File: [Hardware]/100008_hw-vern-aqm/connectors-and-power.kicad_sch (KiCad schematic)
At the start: 16 parts

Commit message: end of day work
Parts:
- added J?: Conn_01x03_Pin, symbol Connector:Conn_01x03_Pin
- added J?: Conn_01x14_Socket, symbol Connector:Conn_01x14_Socket
- added R? (x2): 0R0, Resistor_SMD:R_0603_1608Metric, symbol Device:R
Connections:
- net +3V3: now also R?.2
- net GND: now also J?.2 (Pin_2), J?.3 (Pin_3)
- net VBUS: now also R?.2
- net I2C_SDA: now reaches J?.3 (Pin_3)
- net I2C_SCL: now reaches J?.4 (Pin_4)
- new net: J?.1 (Pin_1), R?.1, R?.1
- new net LCD_BACKLIGHT: J?.8 (Pin_8)
- new net LCD_DC/RS: J?.5 (Pin_5)
- new net LCD_RESET: J?.4 (Pin_4)
- new net SPI_MISO: J?.13 (Pin_13)
- new net SPI_MOSI: J?.12 (Pin_12), J?.6 (Pin_6)
- new net SPI_SCK: J?.10 (Pin_10), J?.7 (Pin_7)
- new net SPI_nCS_LCD: J?.3 (Pin_3)
- new net SPI_nCS_TOUCH: J?.11 (Pin_11)
- new net UART0_RX: J?.2 (Pin_2)
- new net UART0_TX: J?.1 (Pin_1)
- no-connect marks 0 -> 4
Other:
- note added: "LCD Display pin header connector - ILI9488 driver"
- note added: "Sensirion SEN54 connector - JST GH 1.25mm"
- note added: "UART Programming header"
- note added: "USB-C Input and data connector"
- moved on the sheet: F?, J?, R?

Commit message: mid day progress
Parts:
- removed J?: USB_C_Receptacle_USB2.0_14P, symbol Connector:USB_C_Receptacle_USB2.0_14P
- added C?: 1u, Capacitor_SMD:C_0805_2012Metric, symbol Device:C
- added D?: ESD5Z3V3, Diode_SMD:D_SOD-523, symbol Diode:ESD5Zxx
- added D?: ESD321, Diode_SMD:D_SOD-523, symbol Diode:ESD5Zxx
- added J?: USB_C_Receptacle_USB2.0_16P, symbol Connector:USB_C_Receptacle_USB2.0_16P
- added R?: 0R0, Resistor_SMD:R_0603_1608Metric, symbol Device:R
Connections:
- net +3V3: now also R?.2; no longer U?.2 (VO)
- net GND: now also J?.A1 (GND), J?.A12 (GND), J?.B1 (GND), J?.B12 (GND), J?.S1 (SHIELD)
- net at R?.1: now also J?.B5 (CC2)
- net at F?.1: now also J?.A4 (VBUS), J?.A9 (VBUS), J?.B4 (VBUS), J?.B9 (VBUS)
- net at R?.1: now also J?.A5 (CC1)
- net at R?.1: now also J?.A6 (D+), J?.B6 (D+)
- net at R?.1: now also J?.A7 (D-), J?.B7 (D-)
- new net: R?.1, U?.2 (VO)
- no-connect marks 4 -> 6
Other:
- moved on the sheet: C?, J?, R?, U?

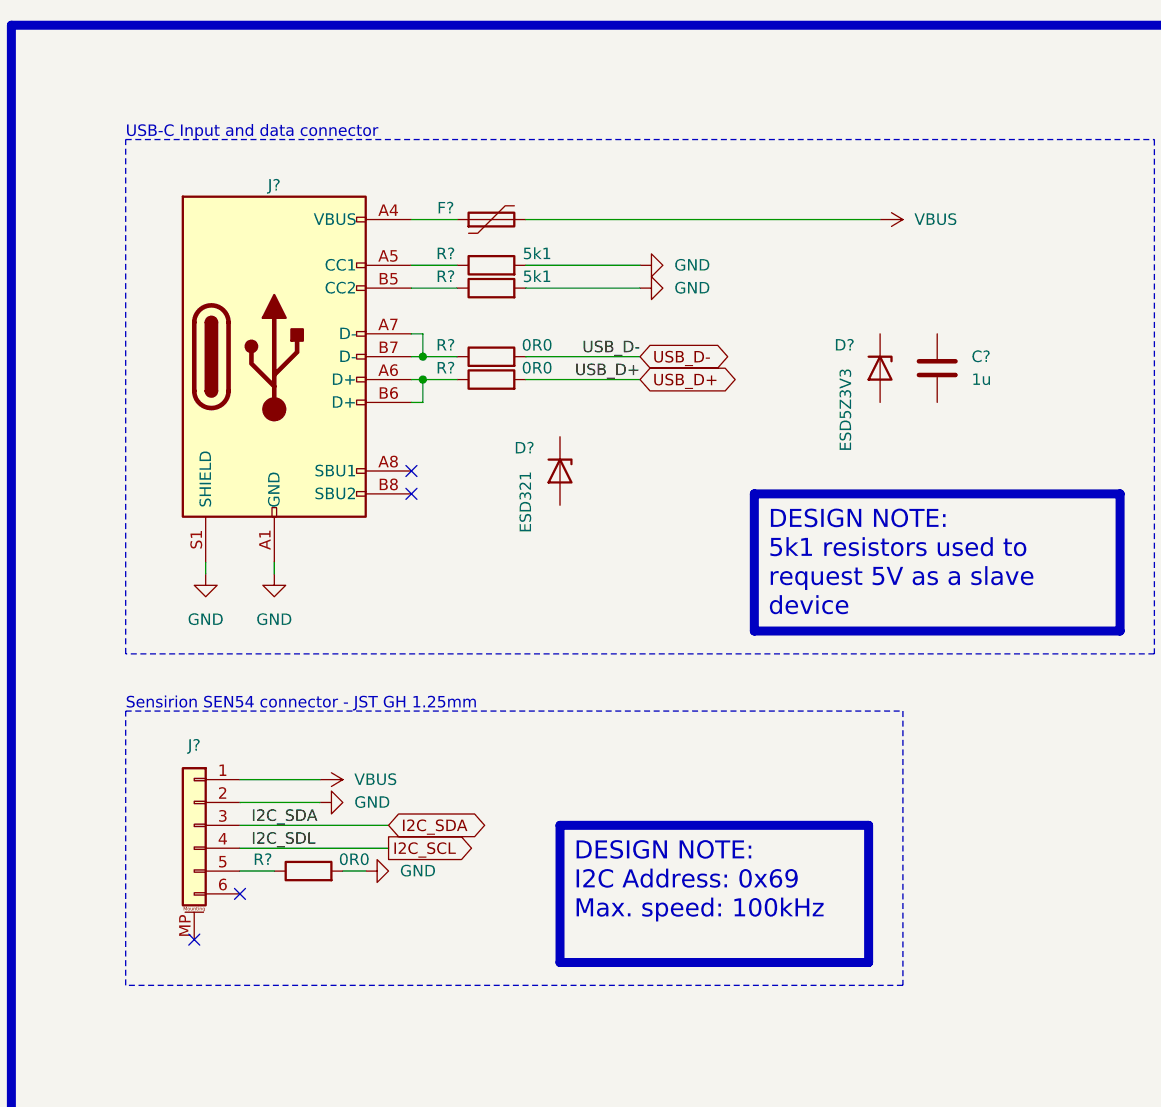
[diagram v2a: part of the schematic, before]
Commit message: added block diagram
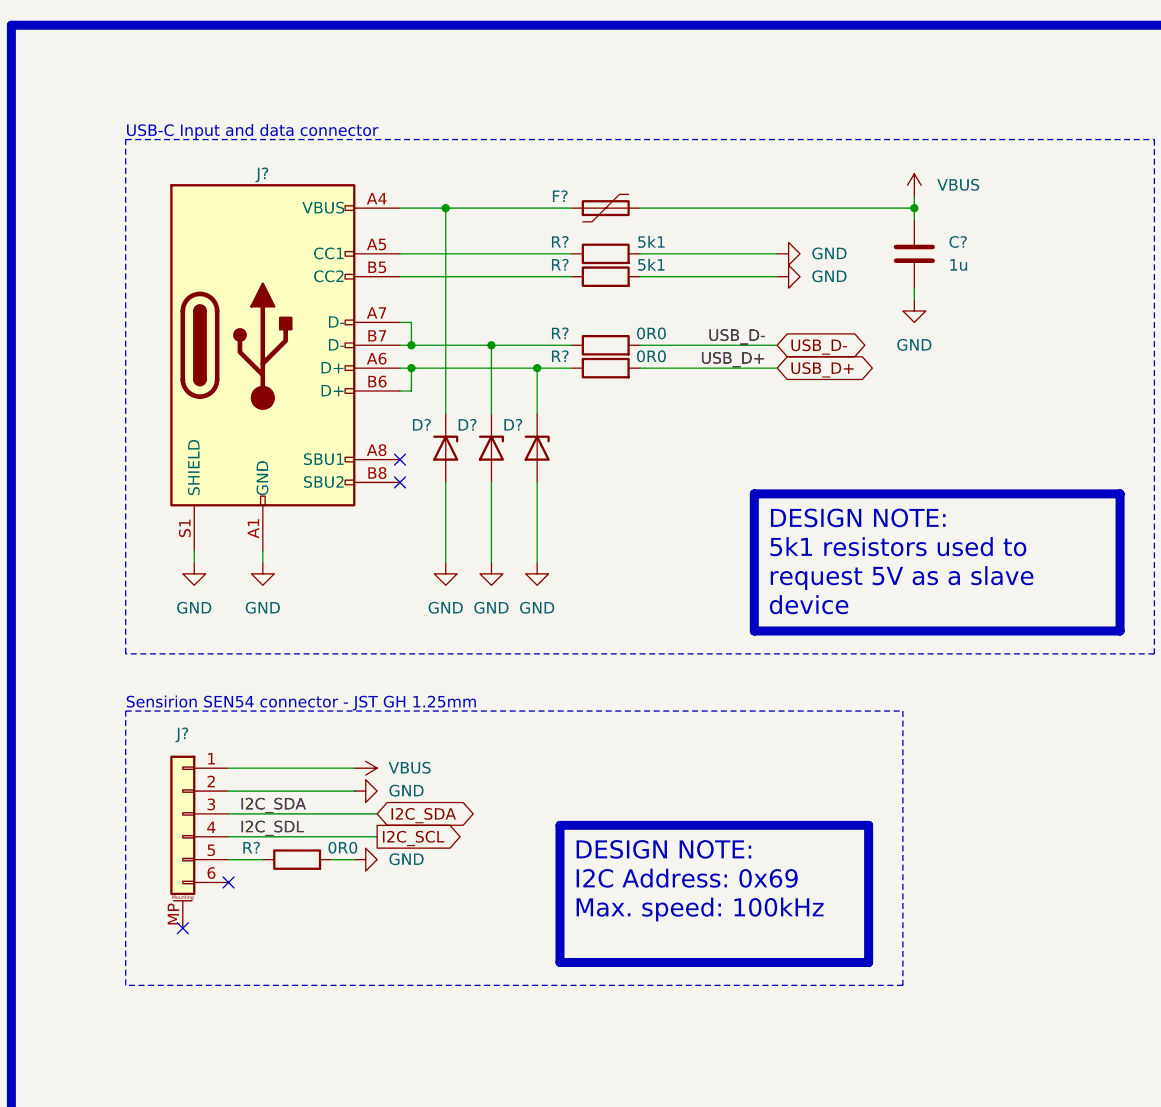
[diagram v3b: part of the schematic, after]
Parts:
- removed C?: 1u, Capacitor_SMD:C_0805_2012Metric, symbol Device:C
- removed D?: ESD5Z3V3, Diode_SMD:D_SOD-523, symbol Diode:ESD5Zxx
- removed D?: ESD321, Diode_SMD:D_SOD-523, symbol Diode:ESD5Zxx
- removed F?: Polyfuse, symbol Device:Polyfuse
- removed J?: USB_C_Receptacle_USB2.0_16P, symbol Connector:USB_C_Receptacle_USB2.0_16P
- removed J?: Conn_01x06_MountingPin, Connector_JST:JST_GH_BM06B-GHS-TBT_1x06-1MP_P1.25mm_Vertical, symbol Connector_Generic_MountingPin:Conn_01x06_MountingPin
- removed R? (x2): 5k1, Resistor_SMD:R_0603_1608Metric, symbol Device:R
- removed R? (x3): 0R0, Resistor_SMD:R_0603_1608Metric, symbol Device:R
- added C?: 1u, Capacitor_SMD:C_0805_2012Metric, symbol Device:C
- added D? (x2): ESD321, Diode_SMD:D_SOD-523, symbol Diode:ESD5Zxx
- added D?: ESD5Z3V3, Diode_SMD:D_SOD-523, symbol Diode:ESD5Zxx
- added F?: Polyfuse, symbol Device:Polyfuse
- added J?: Conn_01x06_MountingPin, Connector_JST:JST_GH_BM06B-GHS-TBT_1x06-1MP_P1.25mm_Vertical, symbol Connector_Generic_MountingPin:Conn_01x06_MountingPin
- added J?: USB_C_Receptacle_USB2.0_16P, symbol Connector:USB_C_Receptacle_USB2.0_16P
- added R? (x2): 5k1, Resistor_SMD:R_0603_1608Metric, symbol Device:R
- added R? (x3): 0R0, Resistor_SMD:R_0603_1608Metric, symbol Device:R
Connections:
- net GND: now also C?.2, D?.2 (A), D?.2 (A), D?.2 (A), J?.2 (Pin_2), J?.A1 (GND), J?.A12 (GND), J?.B1 (GND), J?.B12 (GND), J?.S1 (SHIELD), R?.2, R?.2, R?.2
- net I2C_SCL: now also J?.4 (Pin_4)
- net I2C_SDA: now also J?.3 (Pin_3)
- net USB_D+: now also R?.2
- net USB_D-: now also R?.2
- net VBUS: now also C?.1, F?.2, J?.1 (Pin_1)
- new net: D?.1 (K), J?.A7 (D-), J?.B7 (D-), R?.1
- new net: J?.B5 (CC2), R?.1
- new net: J?.5 (Pin_5), R?.1
- new net: D?.1 (K), J?.A6 (D+), J?.B6 (D+), R?.1
- new net: D?.1 (K), F?.1, J?.A4 (VBUS), J?.A9 (VBUS), J?.B4 (VBUS), J?.B9 (VBUS)
- new net: J?.A5 (CC1), R?.1
